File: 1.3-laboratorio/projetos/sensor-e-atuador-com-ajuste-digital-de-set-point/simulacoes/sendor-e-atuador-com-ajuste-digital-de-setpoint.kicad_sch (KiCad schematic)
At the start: 30 parts, among them U1 OPAMP, U2 OPAMP, U3 OPAMP

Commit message: Roteiro sobre Comparadores elaborado. Atualizações do projeto Sensor e Atuador com Ajuste Digital de Set-Point.
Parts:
- removed R12: GL10537-1, symbol ldr-ponte-rescue:R_PHOTO-Device
- added R22: R_Photo, symbol Device:R_Photo
- R1, R10, R2, R4, R8: Spice_Model 2.2k -> 22k
- R11: Spice_Model Rb -> 22k
- R12: renamed from R13; Spice_Model 10k -> 120k
- R14: renamed from R15; Spice_Model 10k -> 220k
- R15: renamed from R16; Spice_Model 10k -> 100k
- R17: renamed from R18; Spice_Model 8.2k -> 160k
- R18: renamed from R19; value 1k -> 10k
- R19: renamed from R20; Spice_Model 2.7k -> 15k
- R20: renamed from R21; Spice_Model 10k -> 100k
- R3, R5, R9: Spice_Model 1.1k -> 11k
- V2: Spice_Model dc Vf pulse(0 Vf 50m ts td 50m 100m) -> dc Vf pwl(0 0 50m 0 '50m+ts' Vf 62.5m Vf '62.5m+td' 0 r =0)
- V3: Spice_Model dc Vf pulse(0 Vf 25m ts td 25m 50m) -> dc Vf pwl(0 0 25m 0 '25m+ts' Vf 50m Vf '50m+td' 0 62.5m 0 r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
- V4: Spice_Model dc Vf pulse(0 Vf 12.5m ts td 12.5m 25m) -> dc Vf pwl(0 0 12.5m 0 '12.5m+ts' Vf 25m Vf '25m+td' 0 37.5m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
- renumbered R14 to R13, R17 to R16, R22 to R21
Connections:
- net PWB is gone; now on net Vldr: R11.2, U1.1 (+)
- net 0: now also R11.1, R6.1; no longer R2.2, R4.2, R7.2, R8.2
- net A: now also R10.2
- net B: now also R8.2
- net C: now also R4.2
- net D: now also R2.2
- net VCC: now also R7.2, R22.2; no longer R10.2, R11.1, R6.1
- net Vldr: now also R22.1; no longer R13.2, R16.2, U1.3
- net Vu3+: now reaches R19.2, R20.1, U3.1 (+)
- net PWA renamed Vref_ldr
- new net Vsensor: R13.2, R16.2, U1.3
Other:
- moved on the sheet: R19, R20, R21, U3, V3, V4, V5

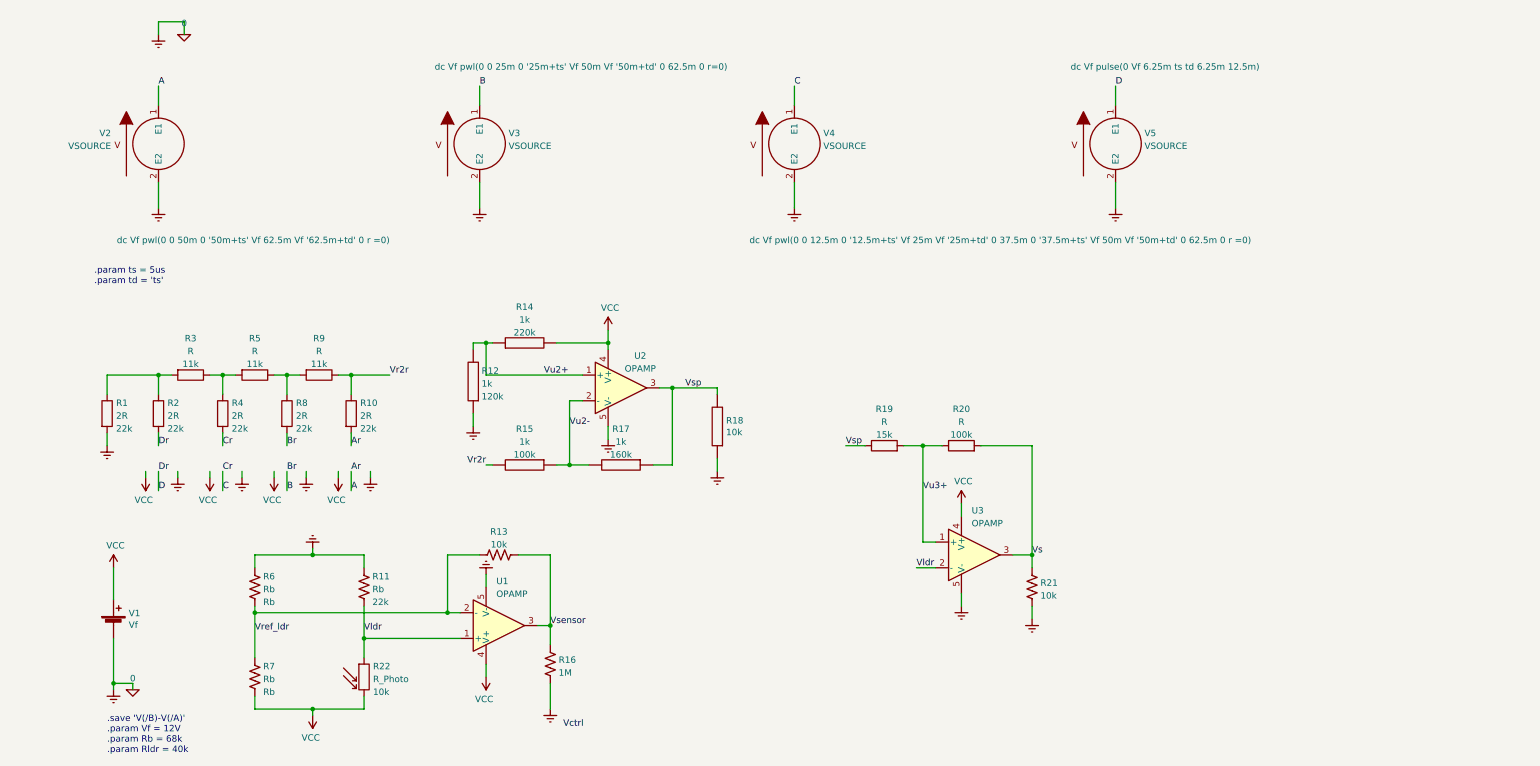
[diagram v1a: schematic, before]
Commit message: Provas. Simulações e gráficos. Gráfico com histerese. Redimensionamento e reposicionamento de janela com gráficos: ver arquivo .cir.
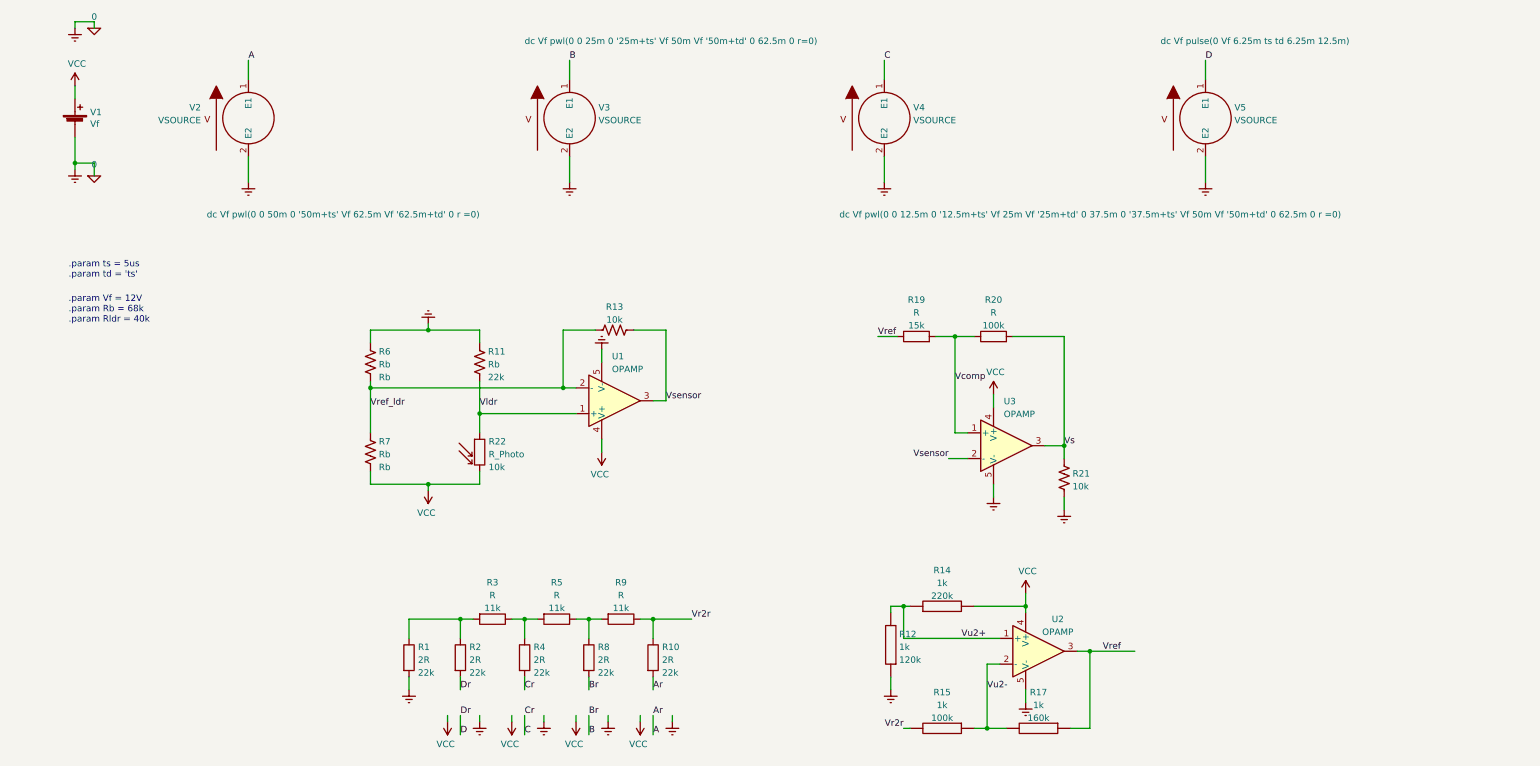
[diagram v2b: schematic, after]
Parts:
- removed R16: 1M, symbol Device:R_US
- removed R18: 10k, symbol pspice:R
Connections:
- net Vldr: no longer U3.2 (-)
- net Vsensor: now also U3.2 (-)
- net Vsp renamed Vref
- net Vu3+ renamed Vcomp
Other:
- note added: ".param Vf = 12V .param Rb = 68k .param Rldr = 40k"
- note removed: ".save 'V(/B)-V(/A)' .param Vf = 12V .param Rb = 68k .param Rldr = 40k"
- moved on the sheet: R1, R10, R11, R12, R13, R14, R15, R17, R19, R2, R20, R21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
